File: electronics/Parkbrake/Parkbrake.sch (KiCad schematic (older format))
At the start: 11 parts, among them P1 Conn48pin

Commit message: Fixes to Bat switch and polarity protection
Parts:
- added VR? (x2): VR, symbol VR
- Q?: value Q_PMOS_GDS -> P-ch -40V 0.0035ohm; farnell (none) -> 2480840; part (none) -> 2480840
- Q? (x2): value Q_PMOS_GDS -> P-ch -40V 0.0035ohm; farnell (none) -> 2480840; part (none) -> PD90P04P4-05
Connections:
- wire segments 12 -> 13
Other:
- note added: "Batt switch off and polarity protection"
- note added: "Polarity protection ignition"
- moved on the sheet: D?, Q?, R?

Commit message: Add currentlimit latching to avaoid current limit oscilation Start a mcu schema part
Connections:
- net labels added: +12V_Bat, CAN_HI, CAN_LO, LeftFrontMotor+, LeftFrontMotor-, LeftRearMotor+, LeftRearMotor-, RightFrontMotor+, RightFrontMotor-, RightRearMotor+, RightRearMotor-
- wire segments 13 -> 35
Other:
- moved on the sheet: P1
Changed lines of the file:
@@
 $Descr A4 11693 8268
 encoding utf-8
-Sheet 1 5
+Sheet 1 6
 Title ""
 Date ""
@@
 L Conn48pin P1
 U 1 1 56FEAA1E
-P 1075 2225
-F 0 "P1" H 1000 3850 60  0000 L CNN
-F 1 "Conn48pin" H 900 3750 60  0000 L CNN
-F 2 "" H 1225 2525 60  0000 C CNN
-F 3 "" H 1225 2525 60  0000 C CNN
-	1    1075 2225
+P 2150 2225
+F 0 "P1" H 2075 3850 60  0000 L CNN
+F 1 "Conn48pin" H 1975 3750 60  0000 L CNN
+F 2 "" H 2300 2525 60  0000 C CNN
+F 3 "" H 2300 2525 60  0000 C CNN
+	1    2150 2225
 	1    0    0    -1
 $EndComp
 $Sheet
-S 6500 2600 1525 1450
+S 8875 2600 1525 1450
 U 570483C1
 F0 "H-Bridge_logic" 60
@@
 $EndSheet
 $Sheet
-S 6500 1000 1525 850
+S 8875 1000 1525 850
 U 57088F10
 F0 "PowerRegulators" 60
@@
 $EndComp
 Connection ~ 2725 6100
+Connection ~ 2050 1025
+Wire Wire Line
+	1800 1025 1800 1325
+Wire Wire Line
+	2050 1025 2050 1175
+Connection ~ 1800 1175
+Connection ~ 1800 1025
+Wire Wire Line
+	1575 1025 2300 1025
+$Comp
+L GNDPWR #PWR?
+U 1 1 570235BF
+P 1575 1025
+F 0 "#PWR?" H 1575 825 50  0001 C CNN
+F 1 "GNDPWR" H 1582 1099 50  0000 C CNN
+F 2 "" H 1575 975 50  0000 C CNN
+F 3 "" H 1575 975 50  0000 C CNN
+	1    1575 1025
+	1    0    0    -1
+$EndComp
+Wire Wire Line
+	2300 1475 1800 1475
+Wire Wire Line
+	2050 1475 2050 1325
+Wire Wire Line
+	2300 1175 2300 1475
+Connection ~ 2050 1475
+Connection ~ 2300 1325
+Wire Wire Line
+	2300 1175 2650 1175
+Text Label 2650 1175 0    60   ~ 0
++12V_Bat
+Wire Wire Line
+	1800 1625 2675 1625
+Connection ~ 2050 1625
+Connection ~ 2300 1625
+Wire Wire Line
+	1625 1775 2300 1775
+Connection ~ 2050 1775
+Connection ~ 1800 1775
+Wire Wire Line
+	1800 1925 2675 1925
+Connection ~ 2050 1925
+Connection ~ 2300 1925
+Wire Wire Line
+	1625 2075 2300 2075
+Connection ~ 2050 2075
+Connection ~ 1800 2075
+Wire Wire Line
+	1800 2225 2675 2225
+Connection ~ 2050 2225
+Connection ~ 2300 2225
+Wire Wire Line
+	1625 2375 2300 2375
+Connection ~ 2050 2375
+Connection ~ 1800 2375
+Wire Wire Line
+	1800 3025 2675 3025
+Connection ~ 2050 3025
+Connection ~ 2300 3025
+Wire Wire Line
+	1625 3175 2300 3175
+Connection ~ 2050 3175
+Connection ~ 1800 3175
+Text GLabel 2675 1625 2    60   Input ~ 0
+LeftFrontMotor+
+Text GLabel 1625 1775 0    60   Input ~ 0
+LeftFrontMotor-
+Text GLabel 2675 1925 2    60   Input ~ 0
+RightFrontMotor+
+Text GLabel 1625 2075 0    60   Input ~ 0
+RightFrontMotor-
+Text GLabel 2675 2225 2    60   Input ~ 0
+LeftRearMotor+
+Text GLabel 1625 2375 0    60   Input ~ 0
+LeftRearMotor-
+Text GLabel 2675 3025 2    60   Input ~ 0
+RightRearMotor+
+Text GLabel 1625 3175 0    60   Input ~ 0
+RightRearMotor-
+Wire Wire Line
+	2300 3325 2675 3325
+Text Label 2675 3325 0    60   ~ 0
++12V_IGN
+Wire Wire Line
+	2050 3325 2050 3250
+Wire Wire Line
+	2050 3250 2625 3250
+Wire Wire Line
+	2625 3250 2625 3150
+Wire Wire Line
+	2625 3150 3225 3150
+$Comp
+L GND #PWR?
+U 1 1 570245AD
+P 3225 3150
+F 0 "#PWR?" H 3225 2900 50  0001 C CNN
+F 1 "GND" H 3233 2977 50  0001 C CNN
+F 2 "" H 3225 3150 50  0000 C CNN
+F 3 "" H 3225 3150 50  0000 C CNN
+	1    3225 3150
+	1    0    0    -1
+$EndComp
+Wire Wire Line
+	1800 3325 1625 3325
+Wire Wire Line
+	1800 3475 1625 3475
+Text GLabel 1625 3325 0    60   Input ~ 0
+CAN_HI
+Text GLabel 1625 3475 0    60   Input ~ 0
+CAN_LO
+$Sheet
+S 5675 2450 1250 1375
+U 570A3FC3
+F0 "microcontroller" 60
+F1 "microcontroller.sch" 60
+$EndSheet
 $EndSCHEMATC

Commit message: More work on parkbrake node
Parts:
- removed Q?: P-ch -40V 0.0035ohm, symbol Q_PMOS_GDS
- added Q? (x2): Q_PMOS_GSD, symbol Q_PMOS_GSD
- added R?: 1k, Resistors_SMD:R_0805, symbol R
- added W?: TP_enable_bridge_pwr, symbol TEST_1P
- R? (x2): footprint (none) -> Resistors_SMD:R_0805; farnell (none) -> 9332391; part (none) -> MC01W0805110K
- R?: footprint (none) -> Resistors_SMD:R_0805; farnell (none) -> 9332383; part (none) -> MC01W080511K
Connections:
- net labels added: +12V_Feed, +12V_ign_in, BrakeLight, Enable_Bridge_PWR, LF_wheelsensor_in+, LF_wheelsensor_in-, LR_wheelsensor_in+, LR_wheelsensor_in-, L_wheelsensor_out+, L_wheelsensor_out-, ParkbrakeSwitch_non_invert, Parkbrake_indicator_lamp, RF_wheelsensor_in+, RF_wheelsensor_in-, RR_wheelsensor_in+, RR_wheelsensor_in-, R_wheelsensor_out+, R_wheelsensor_out-, wheelsensor_shielding, ~ParkbrakeSwitch_invert
- net labels removed: +12V_IGN, +12V_IGN_Safe, Enable_12V_power
- wire segments 35 -> 94
- no-connect marks 0 -> 1
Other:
- note added: "Polarity protection ignition and force activate"
- note removed: "Polarity protection ignition"
- moved on the sheet: D?, R?, VR?

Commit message: ordernr, type and footprints for all components
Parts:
- added Ha?: Box, symbol Hardware
- added Ha?: box_endcap, symbol Hardware
- added Ha?: cooloing_fin, symbol Hardware
- added Ha?: fin_left, symbol Hardware
- added Ha?: conn_18pin, symbol Hardware
- added Ha?: conn_30pin, symbol Hardware
- added Ha?: connector_pins, symbol Hardware
- added Ha?: sealplug_need_10, symbol Hardware
- D? (x2): footprint (none) -> Diodes_SMD:SOD-123; farnell (none) -> 2061476; part (none) -> MMSZ5240B
- D?: footprint (none) -> Diodes_SMD:SOD-123; farnell (none) -> 2433353; part (none) -> 1N4148W-E3-08
- Q? (x2): footprint (none) -> TO_SOT_Packages_SMD:TO-252-2Lead
- Q?: value Q_NMOS_GSD -> 2N7002; symbol Q_NMOS_GSD -> BSS138; farnell (none) -> 1510761; part (none) -> 2N7002
- Q?: value Q_PMOS_GSD -> BSS308; farnell (none) -> 2432719; part (none) -> BSS308PE H6327
- Q?: value Q_PMOS_GSD -> BSS308; footprint (none) -> TO_SOT_Packages_SMD:SOT-23; farnell (none) -> 2432719; part (none) -> BSS308PE H6327
- VR? (x2): footprint (none) -> Resistors_SMD:R_1206; farnell 1301938 -> 2346678; part VC120618A400DP -> VCAS120614A300DP
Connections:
- wire segments 94 -> 112
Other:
- moved on the sheet: R?

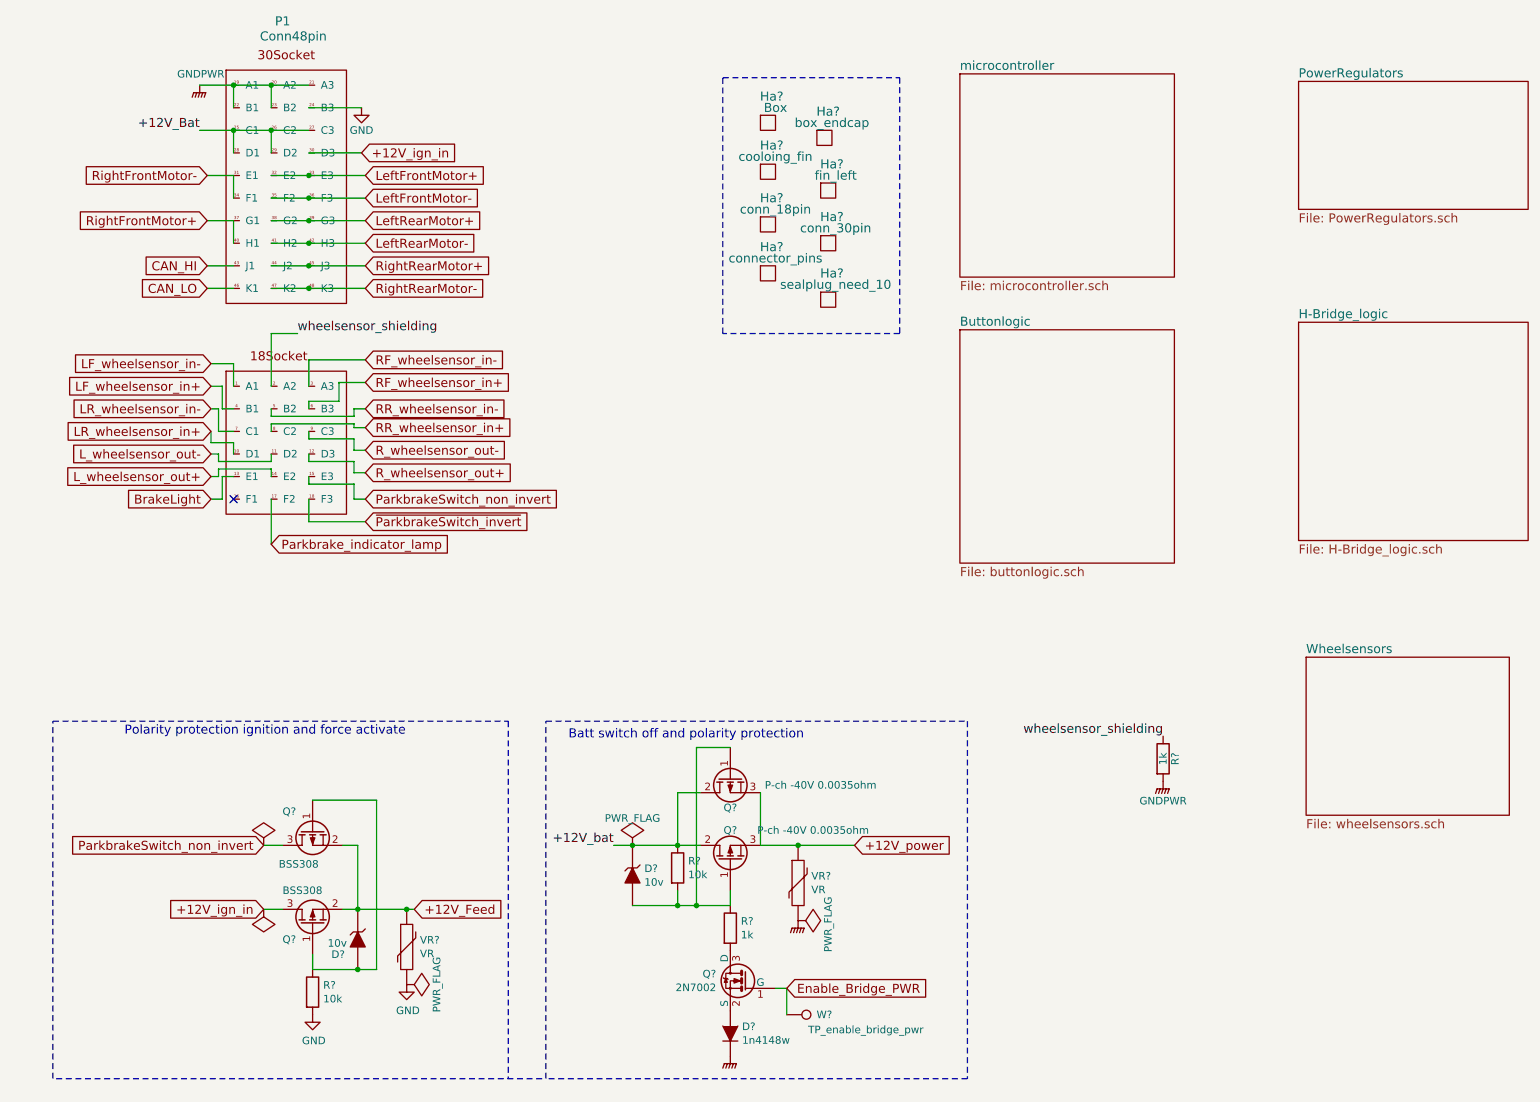
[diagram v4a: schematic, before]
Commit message: Make it pass DRC rule check
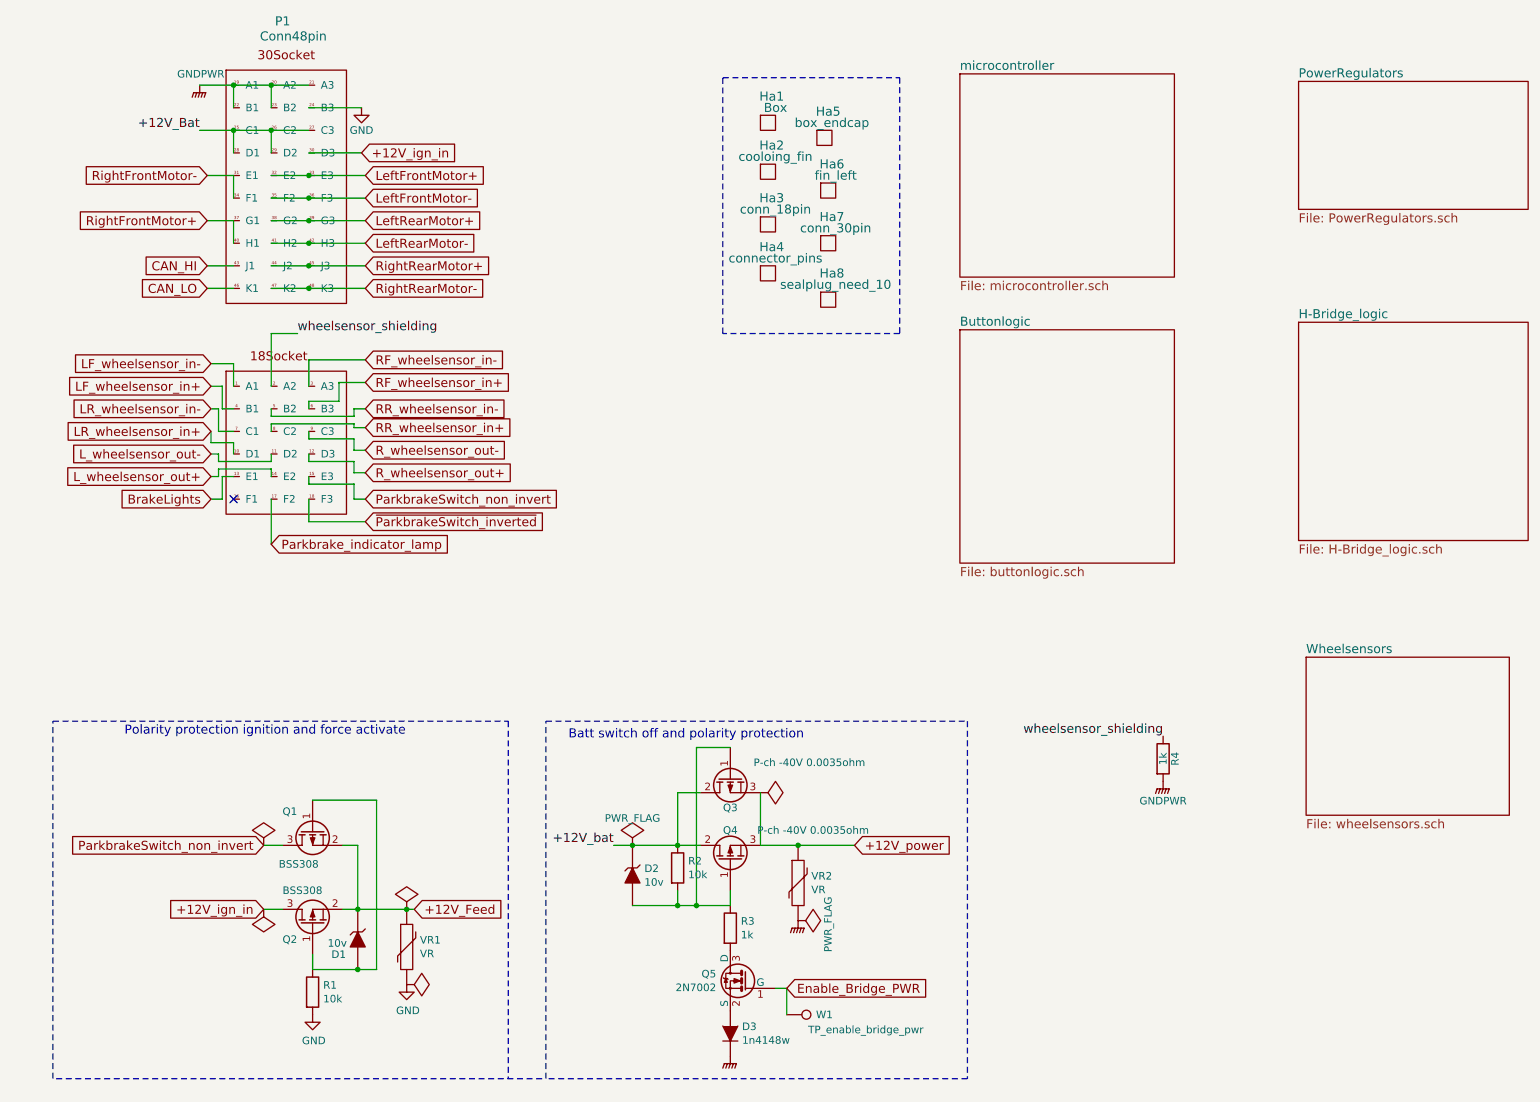
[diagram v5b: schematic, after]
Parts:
- gave numbers to parts that had none: 23
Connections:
- net BrakeLight renamed BrakeLights
- net ~ParkbrakeSwitch_invert renamed ~ParkbrakeSwitch_inverted

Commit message: More fixes and chenged components eat less boardspace
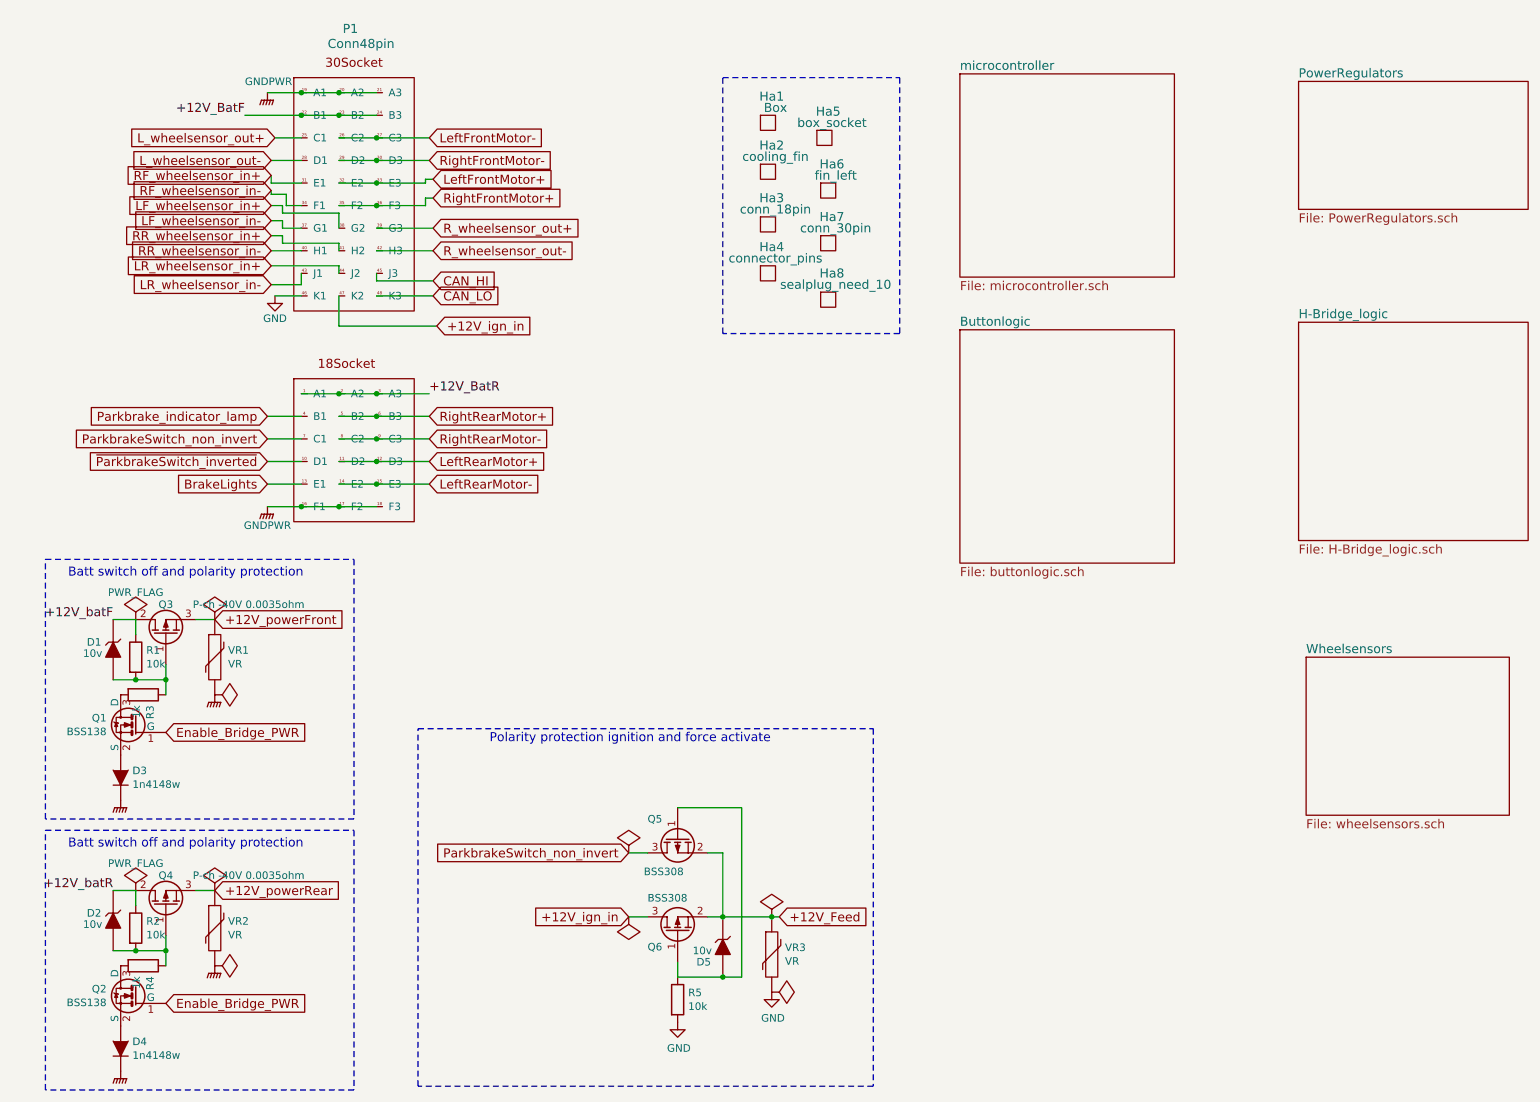
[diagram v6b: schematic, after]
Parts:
- removed Q3: P-ch -40V 0.0035ohm, TO_SOT_Packages_SMD:TO-252-2Lead, symbol Q_PMOS_GDS
- removed W1: TP_enable_bridge_pwr, symbol TEST_1P
- added D2: 10v, Diodes_SMD:SOD-323, symbol ZENER
- added D4: 1n4148w, Diodes_SMD:SOD-323, symbol D
- added Q2: BSS138, TO_SOT_Packages_SMD:SOT-323, symbol BSS138
- added Q4: P-ch -40V 0.0035ohm, TO_SOT_Packages_SMD:TO-252-2Lead, symbol Q_PMOS_GDS
- added R2: 10k, Resistors_SMD:R_0805, symbol R
- added VR2: VR, Resistors_SMD:R_1206, symbol VR
- D1: renamed from D2; footprint Diodes_SMD:SOD-123 -> Diodes_SMD:SOD-323; farnell 2061476 -> 1431190; part MMSZ5240B -> MM3Z10VT1G
- D3: footprint Diodes_SMD:SOD-123 -> Diodes_SMD:SOD-323; farnell 2433353 -> 1466524; part 1N4148W-E3-08 -> 1N4148WS
- D5: renamed from D1; footprint Diodes_SMD:SOD-123 -> Diodes_SMD:SOD-323; farnell 2061476 -> 1431190; part MMSZ5240B -> MM3Z10VT1G
- Ha2: value cooloing_fin -> cooling_fin
- Ha5: value box_endcap -> box_socket
- Q1: renamed from Q5; value 2N7002 -> BSS138; footprint (none) -> TO_SOT_Packages_SMD:SOT-323; farnell 1510761 -> 1907611; part 2N7002 -> BSS138PW
- Q6: renamed from Q2; footprint (none) -> TO_SOT_Packages_SMD:SOT-23
- R4: farnell MC01W080511K -> 9332383; part 9332383 -> MC01W080511K
- renumbered Q4 to Q3, Q1 to Q5, R2 to R1, R1 to R5, VR2 to VR1, VR1 to VR3
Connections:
- net +12V_ign_in: now also P1.47 (K2); no longer P1.30 (D3)
- net CAN_HI: now also P1.45 (J3); no longer P1.43 (J1)
- net CAN_LO: now also P1.48 (K3); no longer P1.46 (K1)
- net Enable_Bridge_PWR: now also Q2.1 (G)
- net GND: now also P1.46 (K1); no longer P1.24 (B3)
- net GNDPWR: now also P1.16 (F1), P1.17 (F2), P1.18 (F3), D4.1 (K), VR2.2; no longer P1.22 (B1), P1.23 (B2), R4.2
- net LF_wheelsensor_in+: now also P1.38 (G2); no longer P1.4 (B1)
- net LF_wheelsensor_in-: now also P1.37 (G1); no longer P1.1 (A1)
- net LR_wheelsensor_in+: now also P1.44 (J2); no longer P1.10 (D1)
- net LR_wheelsensor_in-: now also P1.43 (J1); no longer P1.7 (C1)
- net L_wheelsensor_out+: now also P1.25 (C1); no longer P1.14 (E2)
- net L_wheelsensor_out-: now also P1.28 (D1); no longer P1.11 (D2)
- net LeftFrontMotor-: now also P1.26 (C2), P1.27 (C3); no longer P1.35 (F2), P1.36 (F3)
- net LeftRearMotor+: now also P1.11 (D2), P1.12 (D3); no longer P1.38 (G2), P1.39 (G3)
- net LeftRearMotor-: now also P1.14 (E2), P1.15 (E3); no longer P1.41 (H2), P1.42 (H3)
- net ParkbrakeSwitch_non_invert: now also P1.7 (C1); no longer P1.15 (E3)
- net Parkbrake_indicator_lamp: now also P1.4 (B1); no longer P1.17 (F2)
- net RF_wheelsensor_in+: now also P1.31 (E1); no longer P1.6 (B3)
- net RF_wheelsensor_in-: now also P1.34 (F1); no longer P1.3 (A3)
- net RR_wheelsensor_in+: now also P1.41 (H2); no longer P1.8 (C2)
- net RR_wheelsensor_in-: now also P1.40 (H1); no longer P1.5 (B2)
- net R_wheelsensor_out+: now also P1.39 (G3); no longer P1.12 (D3)
- net R_wheelsensor_out-: now also P1.42 (H3); no longer P1.9 (C3)
- net RightFrontMotor+: now also P1.35 (F2), P1.36 (F3); no longer P1.37 (G1), P1.40 (H1)
- net RightFrontMotor-: now also P1.29 (D2), P1.30 (D3); no longer P1.31 (E1), P1.34 (F1)
- net RightRearMotor+: now also P1.5 (B2), P1.6 (B3); no longer P1.44 (J2), P1.45 (J3)
- net RightRearMotor-: now also P1.8 (C2), P1.9 (C3); no longer P1.47 (K2), P1.48 (K3)
- net ~ParkbrakeSwitch_inverted: now also P1.10 (D1); no longer P1.18 (F3)
- removed net +12V_Bat: P1.25 (C1), P1.26 (C2), P1.27 (C3), P1.28 (D1), P1.29 (D2)
- net +12V_bat renamed +12V_batF
- net +12V_power renamed +12V_powerFront
- net wheelsensor_shielding: no longer names the net of R4.1
- net wheelsensor_shielding: now also D2.2 (A), Q4.1 (G), R2.2; no longer P1.2 (A2)
- new net: Q2.3 (D), R4.2
- new net: D4.2 (A), Q2.2 (S)
- new net +12V_BatF: P1.22 (B1), P1.23 (B2), P1.24 (B3)
- new net +12V_BatR: P1.1 (A1), P1.2 (A2), P1.3 (A3)
- new net +12V_batR: D2.1 (K), Q4.2 (D), R2.1
- new net +12V_powerRear: Q4.3 (S), VR2.1
- no-connect marks 1 -> 0
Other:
- moved on the sheet: D1, D3, D5, P1, Q1, Q3, Q5, Q6, R1, R3, R5, VR1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
